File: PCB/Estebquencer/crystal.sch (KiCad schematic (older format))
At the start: 3 parts

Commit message: Añadido proyecto ST, configuración superficial de todos los periféricos, falta crear los threads en FreeRTOS
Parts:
- 8MHz: symbol Crystal -> Estebquencer-rescue:Crystal
- C? (x2): symbol C -> Estebquencer-rescue:C
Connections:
- wire segments 6 -> 8
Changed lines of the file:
@@
-EESchema Schematic File Version 2
-LIBS:libreria_proyecto
-LIBS:74xgxx
-LIBS:74xx
-LIBS:ac-dc
-LIBS:actel
-LIBS:adc-dac
-LIBS:Altera
-LIBS:analog_devices
-LIBS:analog_switches
-LIBS:atmel
-LIBS:audio
-LIBS:brooktre
-LIBS:cmos4000
-LIBS:cmos_ieee
-LIBS:conn
-LIBS:contrib
-LIBS:cypress
-LIBS:dc-dc
-LIBS:device
-LIBS:digital-audio
-LIBS:diode
-LIBS:display
-LIBS:dsp
-LIBS:elec-unifil
-LIBS:ESD_Protection
-LIBS:ftdi
-LIBS:gennum
-LIBS:graphic
-LIBS:hc11
-LIBS:intel
-LIBS:interface
-LIBS:ir
-LIBS:Lattice
-LIBS:linear
-LIBS:logo
-LIBS:maxim
-LIBS:memory
-LIBS:microchip
-LIBS:microchip_dspic33dsc
-LIBS:microchip_pic10mcu
-LIBS:microchip_pic12mcu
-LIBS:microchip_pic16mcu
-LIBS:microchip_pic18mcu
-LIBS:microchip_pic32mcu
-LIBS:microcontrollers
-LIBS:motor_drivers
-LIBS:motorola
-LIBS:msp430
-LIBS:nordicsemi
-LIBS:nxp_armmcu
-LIBS:onsemi
-LIBS:opto
-LIBS:Oscillators
-LIBS:philips
-LIBS:power
-LIBS:powerint
-LIBS:Power_Management
-LIBS:pspice
-LIBS:references
-LIBS:regul
-LIBS:relays
-LIBS:rfcom
-LIBS:sensors
-LIBS:silabs
-LIBS:siliconi
-LIBS:stm8
-LIBS:stm32
-LIBS:supertex
-LIBS:switches
-LIBS:texas
-LIBS:transf
-LIBS:transistors
-LIBS:ttl_ieee
-LIBS:valves
-LIBS:video
-LIBS:Xicor
-LIBS:xilinx
-LIBS:Zilog
+EESchema Schematic File Version 4
 LIBS:Estebquencer-cache
-EELAYER 25 0
+EELAYER 26 0
 EELAYER END
 $Descr A4 11693 8268
 encoding utf-8
-Sheet 8 9
+Sheet 8 10
 Title ""
 Date ""
@@
 $EndDescr
 $Comp
-L Crystal 8MHz
+L Estebquencer-rescue:Crystal 8MHz
 U 1 1 5875B883
 P 4950 3400
@@
 $EndComp
 $Comp
-L C C?
+L Estebquencer-rescue:C C?
 U 1 1 5875B8B9
 P 4600 3700
@@
 $EndComp
 $Comp
-L C C?
+L Estebquencer-rescue:C C?
 U 1 1 5875B8FC
 P 5250 3700
@@
 $EndComp
 Wire Wire Line
-	4500 3400 4800 3400
+	4500 3400 4600 3400
 Wire Wire Line
 	4600 3400 4600 3550
 Wire Wire Line
-	5100 3400 5350 3400
+	5100 3400 5250 3400
 Wire Wire Line
 	5250 3400 5250 3550
 $Comp
-L GNDREF #PWR?
+L power:GNDREF #PWR?
 U 1 1 5875B99F
 P 4600 4050
@@
 $EndComp
 $Comp
-L GNDREF #PWR?
+L power:GNDREF #PWR?
 U 1 1 5875B9BA
 P 5250 4050
@@
 Connection ~ 5250 3400
 Connection ~ 4600 3400
+Wire Wire Line
+	5250 3400 5350 3400
+Wire Wire Line
+	4600 3400 4800 3400
 $EndSCHEMATC

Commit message: acabado módulo ARM
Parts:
- removed C?: C, symbol Estebquencer-rescue:C
- added C?: 20pF, symbol Estebquencer-rescue:C
- added R?: 1M, symbol Device:R_Small
- C?: value C -> 20pF
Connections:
- net Xin: now also R?.2
- net Xout: now also C?.1, R?.1
- net GNDREF renamed GND
- net GND: now also C?.2
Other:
- moved on the sheet: 8MHz, C?
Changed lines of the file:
@@
 EELAYER 26 0
 EELAYER END
-$Descr A4 11693 8268
+$Descr User 5906 4000
 encoding utf-8
-Sheet 8 10
+Sheet 7 10
 Title ""
 Date ""
@@
 L Estebquencer-rescue:Crystal 8MHz
 U 1 1 5875B883
-P 4950 3400
-F 0 "8MHz" H 4950 3550 50  0000 C CNN
-F 1 "Crystal" H 4950 3250 50  0000 C CNN
-F 2 "" H 4950 3400 50  0000 C CNN
-F 3 "" H 4950 3400 50  0000 C CNN
-	1    4950 3400
+P 2900 1050
+F 0 "8MHz" H 2900 1200 50  0000 C CNN
+F 1 "Crystal" H 2900 1050 50  0001 C CNN
+F 2 "" H 2900 1050 50  0000 C CNN
+F 3 "" H 2900 1050 50  0000 C CNN
+	1    2900 1050
 	1    0    0    -1
 $EndComp
@@
 L Estebquencer-rescue:C C?
 U 1 1 5875B8B9
-P 4600 3700
-F 0 "C?" H 4625 3800 50  0000 L CNN
-F 1 "C" H 4625 3600 50  0000 L CNN
-F 2 "" H 4638 3550 50  0000 C CNN
-F 3 "" H 4600 3700 50  0000 C CNN
-	1    4600 3700
+P 2550 1550
+F 0 "C?" H 2575 1650 50  0000 L CNN
+F 1 "20pF" H 2575 1450 50  0000 L CNN
+F 2 "" H 2588 1400 50  0000 C CNN
+F 3 "" H 2550 1550 50  0000 C CNN
+	1    2550 1550
+	1    0    0    -1
+$EndComp
+Wire Wire Line
+	2450 1050 2550 1050
+Wire Wire Line
+	3050 1050 3200 1050
+Text HLabel 2450 1050 0    60   Input ~ 0
+Xin
+Text HLabel 3300 1050 2    60   Input ~ 0
+Xout
+Connection ~ 3200 1050
+Connection ~ 2550 1050
+Wire Wire Line
+	3200 1050 3300 1050
+Wire Wire Line
+	2550 1050 2750 1050
+$Comp
+L power:GND #PWR?
+U 1 1 5E3C8828
+P 2550 1800
+F 0 "#PWR?" H 2550 1550 50  0001 C CNN
+F 1 "GND" H 2555 1627 50  0000 C CNN
+F 2 "" H 2550 1800 50  0001 C CNN
+F 3 "" H 2550 1800 50  0001 C CNN
+	1    2550 1800
+	1    0    0    -1
+$EndComp
+$Comp
+L power:GND #PWR?
+U 1 1 5E3C885B
+P 3200 1800
+F 0 "#PWR?" H 3200 1550 50  0001 C CNN
+F 1 "GND" H 3205 1627 50  0000 C CNN
+F 2 "" H 3200 1800 50  0001 C CNN
+F 3 "" H 3200 1800 50  0001 C CNN
+	1    3200 1800
 	1    0    0    -1
 $EndComp
 $Comp
 L Estebquencer-rescue:C C?
-U 1 1 5875B8FC
-P 5250 3700
-F 0 "C?" H 5275 3800 50  0000 L CNN
-F 1 "C" H 5275 3600 50  0000 L CNN
-F 2 "" H 5288 3550 50  0000 C CNN
-F 3 "" H 5250 3700 50  0000 C CNN
-	1    5250 3700
-	1    0    0    -1
-$EndComp
-Wire Wire Line
-	4500 3400 4600 3400
-Wire Wire Line
-	4600 3400 4600 3550
-Wire Wire Line
-	5100 3400 5250 3400
-Wire Wire Line
-	5250 3400 5250 3550
-$Comp
-L power:GNDREF #PWR?
-U 1 1 5875B99F
-P 4600 4050
-F 0 "#PWR?" H 4600 3800 50  0001 C CNN
-F 1 "GNDREF" H 4600 3900 50  0000 C CNN
-F 2 "" H 4600 4050 50  0000 C CNN
-F 3 "" H 4600 4050 50  0000 C CNN
-	1    4600 4050
+U 1 1 5E3CA94D
+P 3200 1550
+F 0 "C?" H 3225 1650 50  0000 L CNN
+F 1 "20pF" H 3225 1450 50  0000 L CNN
+F 2 "" H 3238 1400 50  0000 C CNN
+F 3 "" H 3200 1550 50  0000 C CNN
+	1    3200 1550
 	1    0    0    -1
 $EndComp
 $Comp
-L power:GNDREF #PWR?
-U 1 1 5875B9BA
-P 5250 4050
-F 0 "#PWR?" H 5250 3800 50  0001 C CNN
-F 1 "GNDREF" H 5250 3900 50  0000 C CNN
-F 2 "" H 5250 4050 50  0000 C CNN
-F 3 "" H 5250 4050 50  0000 C CNN
-	1    5250 4050
-	1    0    0    -1
+L Device:R_Small R?
+U 1 1 5E3CAEF4
+P 2900 1300
+F 0 "R?" V 3000 1250 50  0000 C CNN
+F 1 "1M" V 2900 1300 50  0000 C CNN
+F 2 "" H 2900 1300 50  0001 C CNN
+F 3 "~" H 2900 1300 50  0001 C CNN
+	1    2900 1300
+	0    1    1    0
 $EndComp
 Wire Wire Line
-	5250 4050 5250 3850
+	2550 1050 2550 1300
 Wire Wire Line
-	4600 3850 4600 4050
-Text HLabel 4500 3400 0    60   Input ~ 0
-Xin
-Text HLabel 5350 3400 2    60   Input ~ 0
-Xout
-Connection ~ 5250 3400
-Connection ~ 4600 3400
+	2800 1300 2550 1300
+Connection ~ 2550 1300
 Wire Wire Line
-	5250 3400 5350 3400
+	2550 1300 2550 1400
 Wire Wire Line
-	4600 3400 4800 3400
+	3000 1300 3200 1300
+Wire Wire Line
+	3200 1050 3200 1300
+Wire Wire Line
+	3200 1400 3200 1300
+Connection ~ 3200 1300
+Wire Wire Line
+	3200 1700 3200 1800
+Wire Wire Line
+	2550 1800 2550 1700
 $EndSCHEMATC

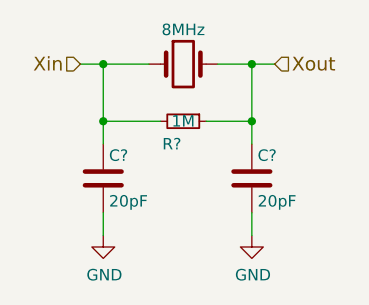
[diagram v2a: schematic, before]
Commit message: Se tuvo que cambiar el sistema de gestión de los LED y pulsadores. Con el charlieplexing no tenía los resultados esperados, así que se le añadió un HT16K33 para hacer las cosas más simples y fluídas. También se usará el mismo IC para la gestión de botones, ya que da opción.
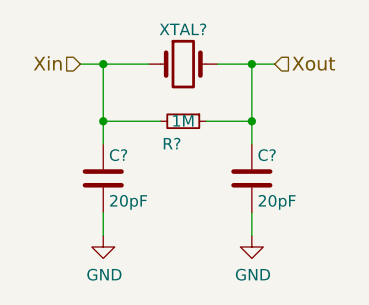
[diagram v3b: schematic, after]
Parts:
- XTAL?: renamed from 8MHz; value Crystal -> 8MHz
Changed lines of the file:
@@
 $Descr User 5906 4000
 encoding utf-8
-Sheet 7 10
+Sheet 6 11
 Title ""
 Date ""
@@
 $EndDescr
 $Comp
-L Estebquencer-rescue:Crystal 8MHz
+L Estebquencer-rescue:Crystal XTAL?
 U 1 1 5875B883
 P 2900 1050
-F 0 "8MHz" H 2900 1200 50  0000 C CNN
-F 1 "Crystal" H 2900 1050 50  0001 C CNN
+F 0 "XTAL?" H 2900 1200 50  0000 C CNN
+F 1 "8MHz" H 2900 1050 50  0001 C CNN
 F 2 "" H 2900 1050 50  0000 C CNN
 F 3 "" H 2900 1050 50  0000 C CNN
@@
 	2550 1050 2750 1050
 $Comp
-L power:GND #PWR?
+L power:GND #PWR0129
 U 1 1 5E3C8828
 P 2550 1800
-F 0 "#PWR?" H 2550 1550 50  0001 C CNN
+F 0 "#PWR0129" H 2550 1550 50  0001 C CNN
 F 1 "GND" H 2555 1627 50  0000 C CNN
 F 2 "" H 2550 1800 50  0001 C CNN
@@
 $EndComp
 $Comp
-L power:GND #PWR?
+L power:GND #PWR0130
 U 1 1 5E3C885B
 P 3200 1800
-F 0 "#PWR?" H 3200 1550 50  0001 C CNN
+F 0 "#PWR0130" H 3200 1550 50  0001 C CNN
 F 1 "GND" H 3205 1627 50  0000 C CNN
 F 2 "" H 3200 1800 50  0001 C CNN

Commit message: Había un pin desconectador de la matriz de LEDs
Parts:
- gave numbers to parts that had none: 4
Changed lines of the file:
@@
 $EndDescr
 $Comp
-L Estebquencer-rescue:Crystal XTAL?
+L Estebquencer-rescue:Crystal XTAL1
 U 1 1 5875B883
 P 2900 1050
-F 0 "XTAL?" H 2900 1200 50  0000 C CNN
+F 0 "XTAL1" H 2900 1200 50  0000 C CNN
 F 1 "8MHz" H 2900 1050 50  0001 C CNN
-F 2 "" H 2900 1050 50  0000 C CNN
+F 2 "" H 2900 1050 50  0001 C CNN
 F 3 "" H 2900 1050 50  0000 C CNN
 	1    2900 1050
@@
 $EndComp
 $Comp
-L Estebquencer-rescue:C C?
+L Estebquencer-rescue:C C13
 U 1 1 5875B8B9
 P 2550 1550
-F 0 "C?" H 2575 1650 50  0000 L CNN
+F 0 "C13" H 2575 1650 50  0000 L CNN
 F 1 "20pF" H 2575 1450 50  0000 L CNN
-F 2 "" H 2588 1400 50  0000 C CNN
+F 2 "" H 2588 1400 50  0001 C CNN
 F 3 "" H 2550 1550 50  0000 C CNN
 	1    2550 1550
@@
 $EndComp
 $Comp
-L Estebquencer-rescue:C C?
+L Estebquencer-rescue:C C14
 U 1 1 5E3CA94D
 P 3200 1550
-F 0 "C?" H 3225 1650 50  0000 L CNN
+F 0 "C14" H 3225 1650 50  0000 L CNN
 F 1 "20pF" H 3225 1450 50  0000 L CNN
-F 2 "" H 3238 1400 50  0000 C CNN
+F 2 "" H 3238 1400 50  0001 C CNN
 F 3 "" H 3200 1550 50  0000 C CNN
 	1    3200 1550
@@
 $EndComp
 $Comp
-L Device:R_Small R?
+L Device:R_Small R20
 U 1 1 5E3CAEF4
 P 2900 1300
-F 0 "R?" V 3000 1250 50  0000 C CNN
+F 0 "R20" V 3000 1250 50  0000 C CNN
 F 1 "1M" V 2900 1300 50  0000 C CNN
 F 2 "" H 2900 1300 50  0001 C CNN
